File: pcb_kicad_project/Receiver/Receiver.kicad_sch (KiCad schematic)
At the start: 37 parts, among them J1 Screw_Terminal_01x02, J2 Screw_Terminal_01x02, J3 Screw_Terminal_01x02, J4 Screw_Terminal_01x02, J5 Conn_02x04_Odd_Even, K1 SRD-12VDC-SL-C, K2 SRD-12VDC-SL-C, Q1 2N3904, Q2 2N3904, U2 B1205S-1WR3

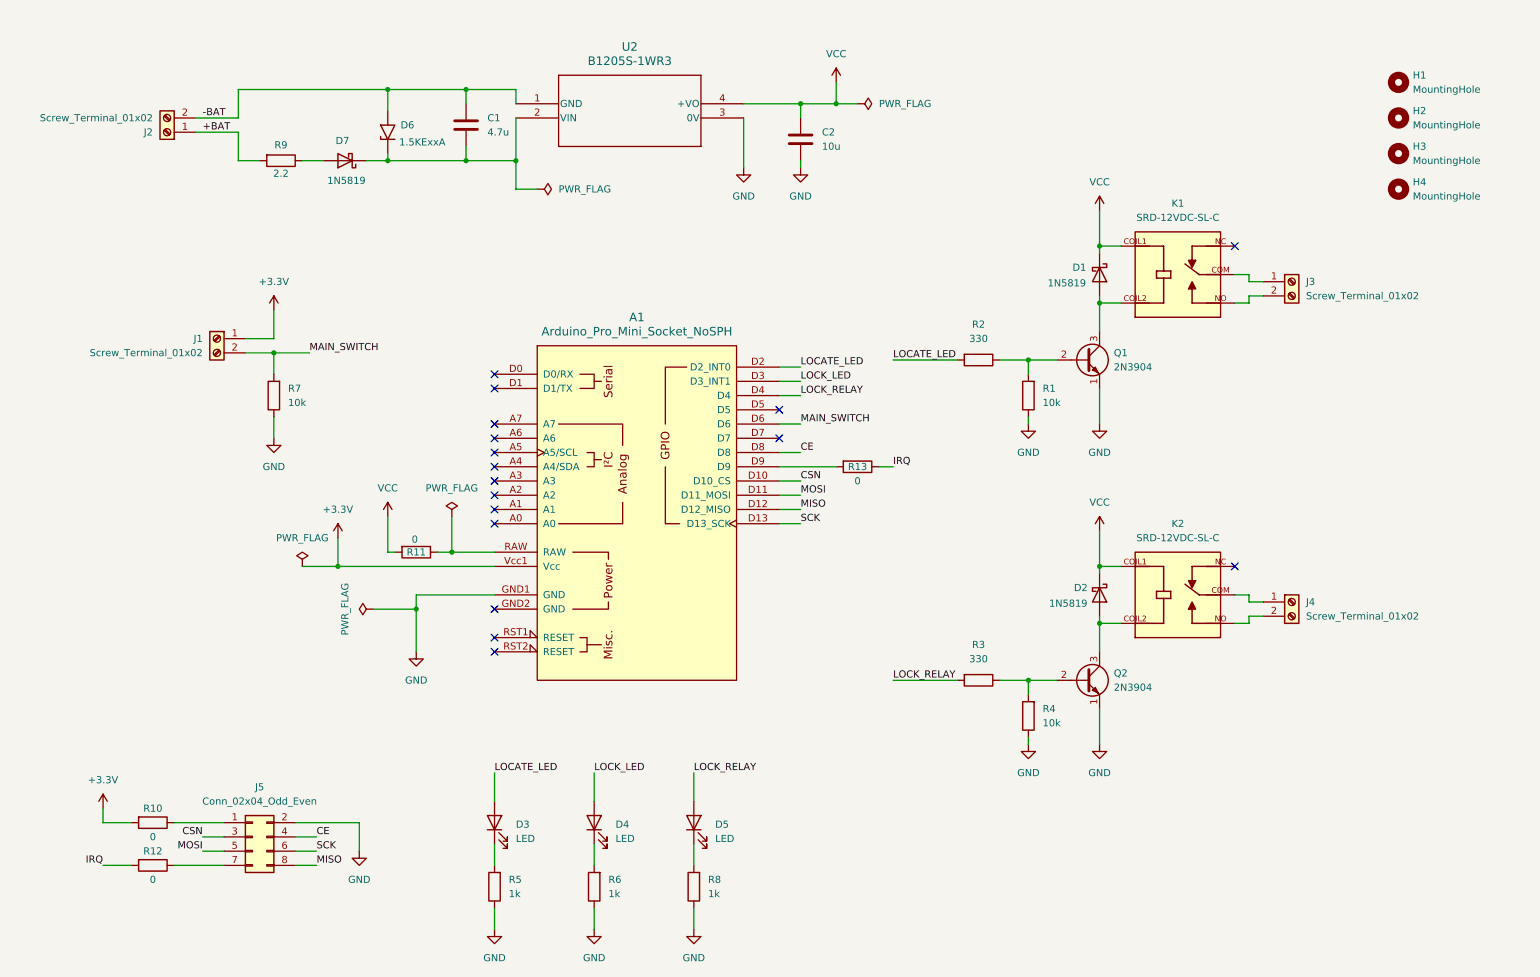
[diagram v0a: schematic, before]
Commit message: update schematic
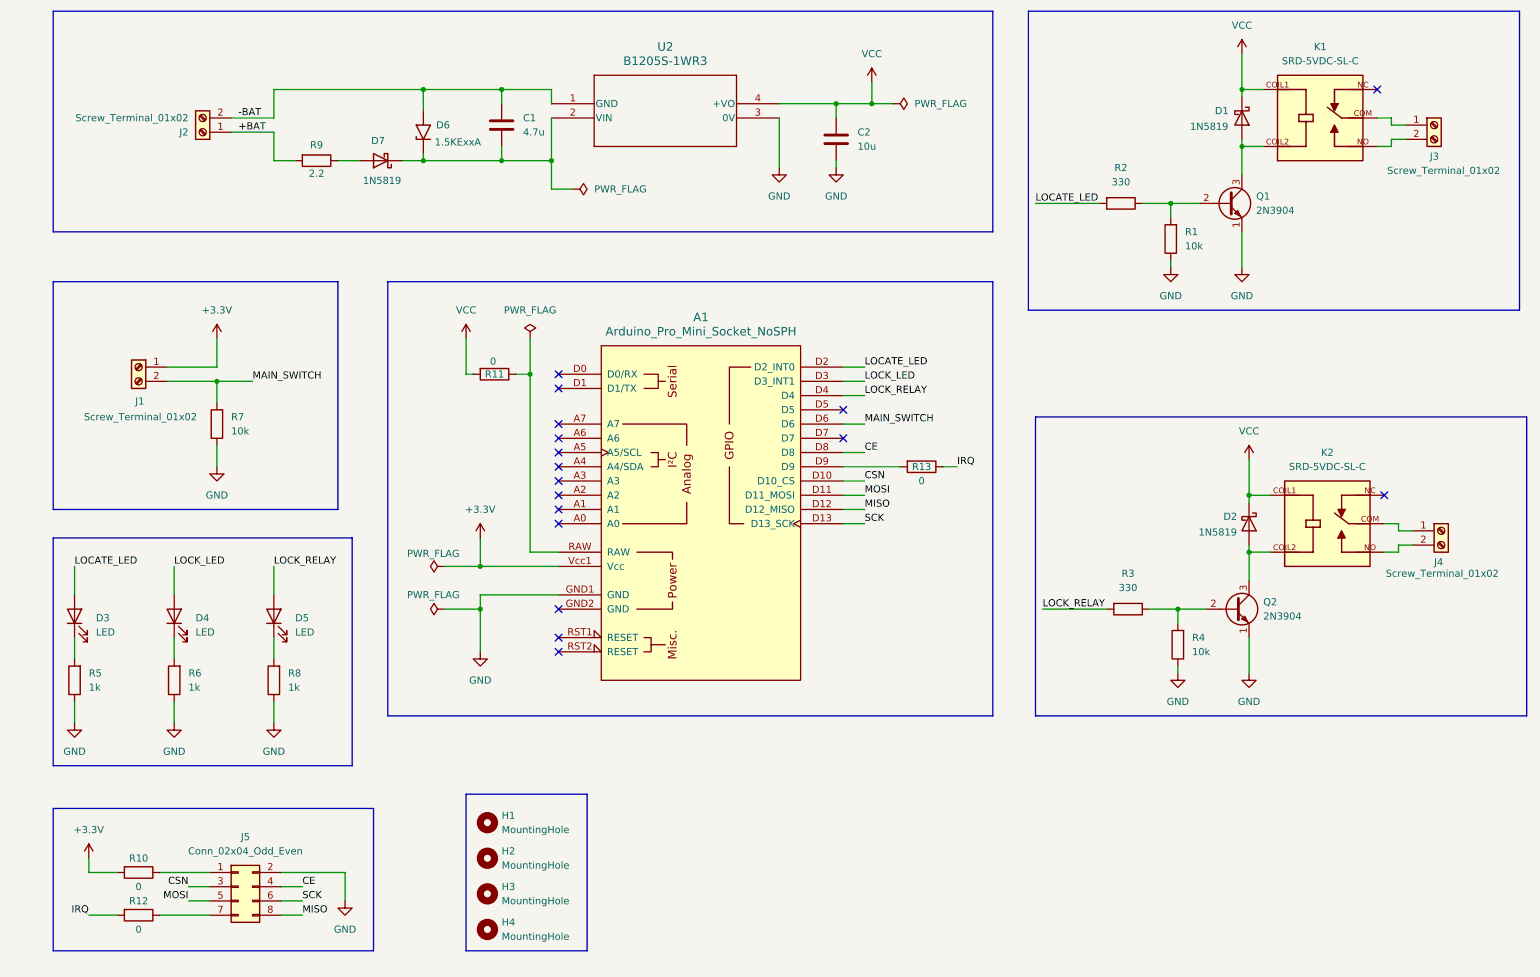
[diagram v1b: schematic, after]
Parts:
- K1, K2: value SRD-12VDC-SL-C -> SRD-5VDC-SL-C
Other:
- moved on the sheet: A1, C1, C2, D1, D2, D3, D4, D5, D6, D7, H1, H2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
